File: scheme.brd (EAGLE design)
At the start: 100 x 80 mm, 49 parts, among them J1 22-05-7048-04, J2 22-05-7028-02

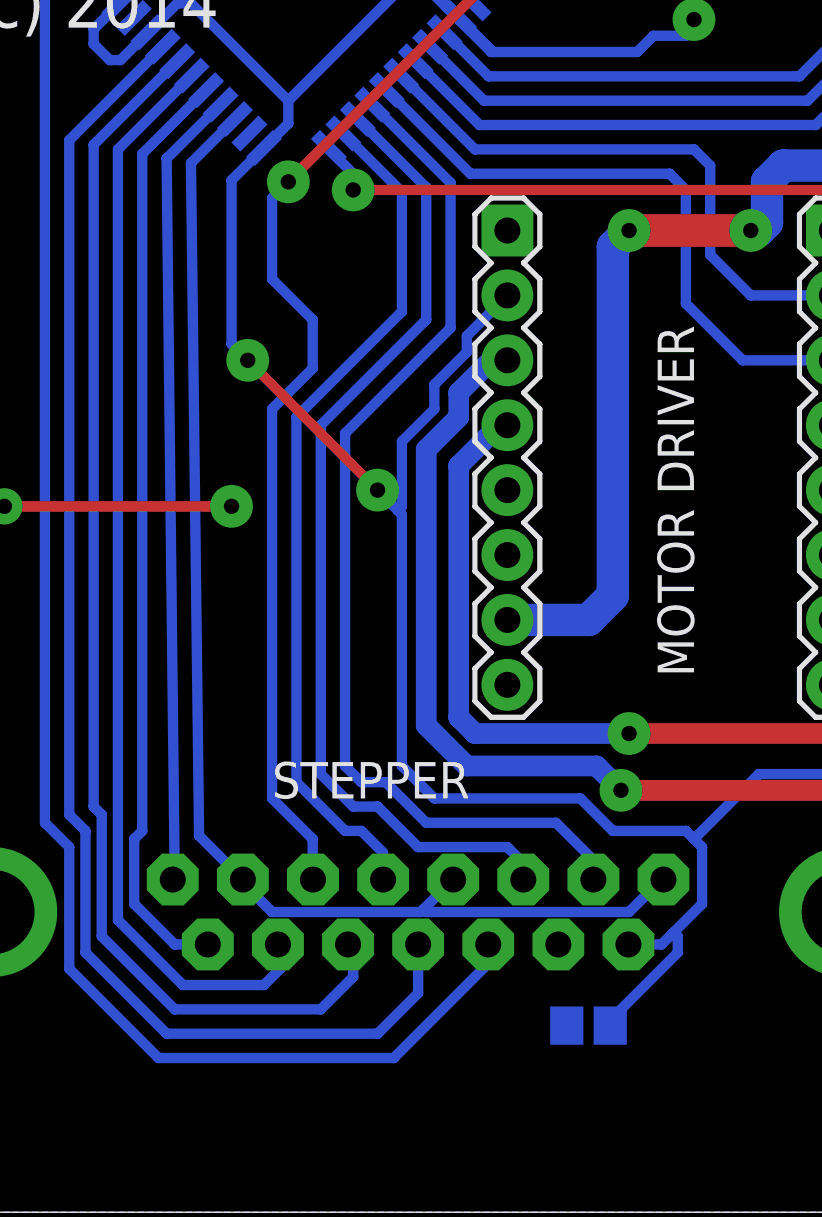
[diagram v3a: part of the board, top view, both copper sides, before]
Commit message: Fix DB-15 connector pinout for driver
Signed-off-by: Nikita 'webconn' Maslov <wkernelteam@gmail.com>
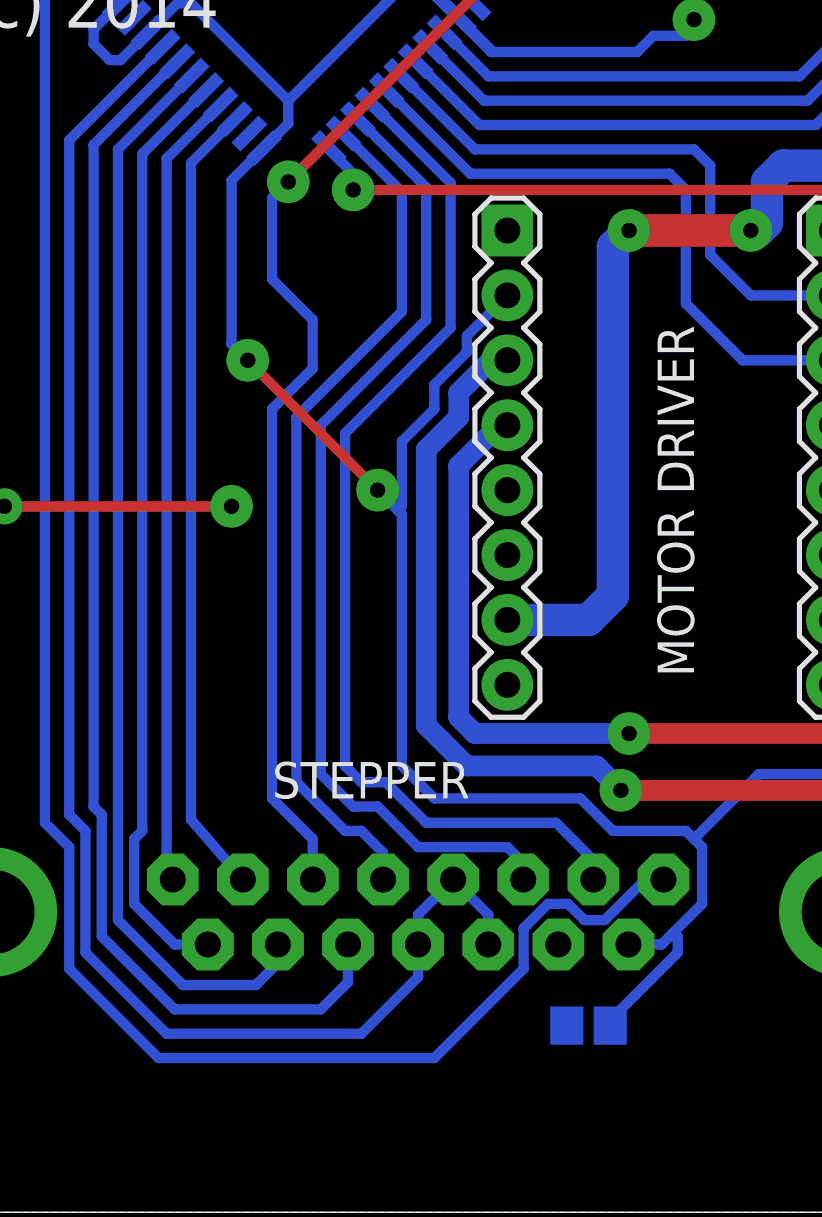
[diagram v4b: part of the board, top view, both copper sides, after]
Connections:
- net RELAY renamed SY_STEP
- net X_DIR renamed SX_STEP
- net X_STEP renamed S_ENABLE
- net Y_DIR renamed SZ_DIR
- net Y_LIM renamed SX_DIR
- net Z_DIR renamed SZ_LIM
- net Z_LIM renamed SY_DIR
- net Z_STEP renamed SY_LIM
- removed net ENABLE: U$1.36, X2.2, X2.5, X2.8
- removed net STOP: U$1.1, X2.13
- removed net Y_STEP: U$1.41, X2.12
- new net SX_LIM: U$1.1, X2.8
- new net SZ_STEP: U$1.36, X2.2
- new net S_RELAY: U$1.41, X2.12, X2.13, X2.5
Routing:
- net SX_LIM: track 0.00 -> 73.3 mm
- net STOP: track 64.4 -> 0.00 mm
- net S_RELAY: track 0.00 -> 60.0 mm
- net Y_STEP: track 54.1 -> 0.00 mm
- net ENABLE: track 50.5 -> 0.00 mm
- net SZ_STEP: track 0.00 -> 31.2 mm

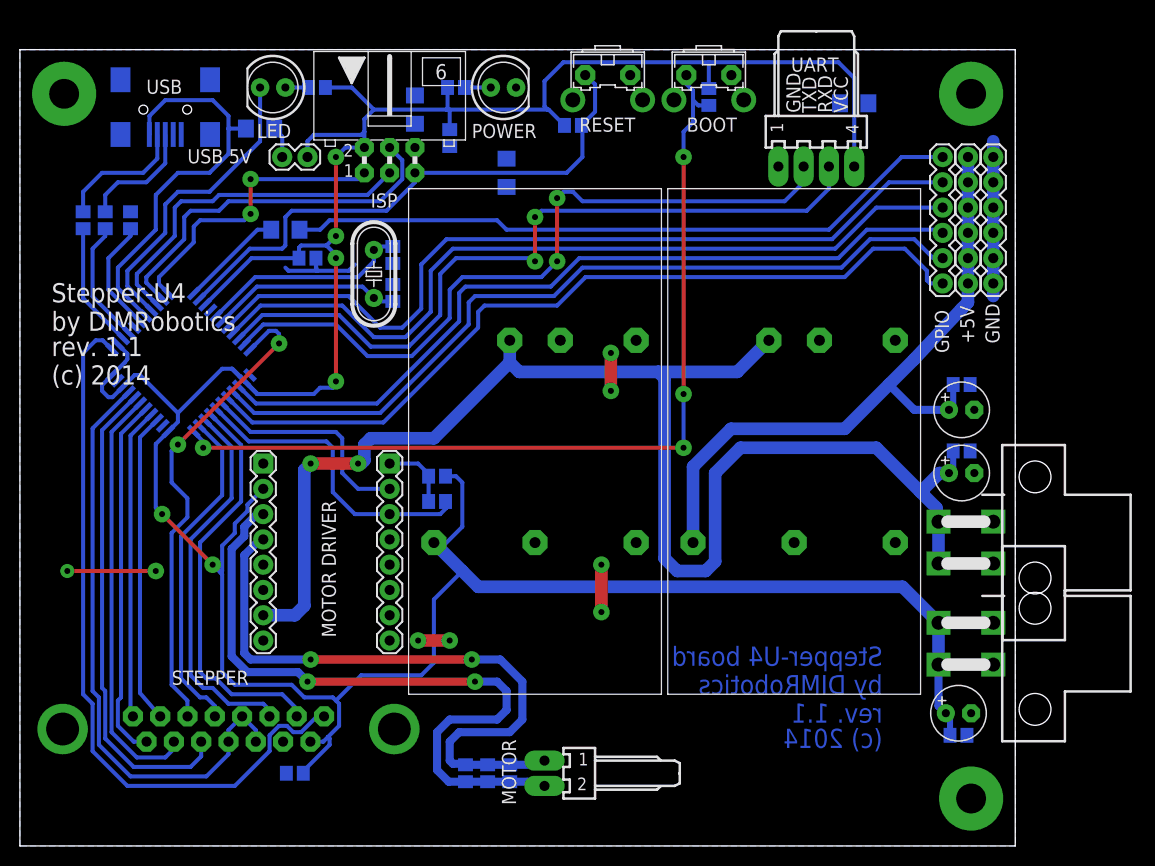
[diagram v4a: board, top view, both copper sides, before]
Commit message: Add D-SUB power jumper
Signed-off-by: Nikita 'webconn' Maslov <wkernelteam@gmail.com>
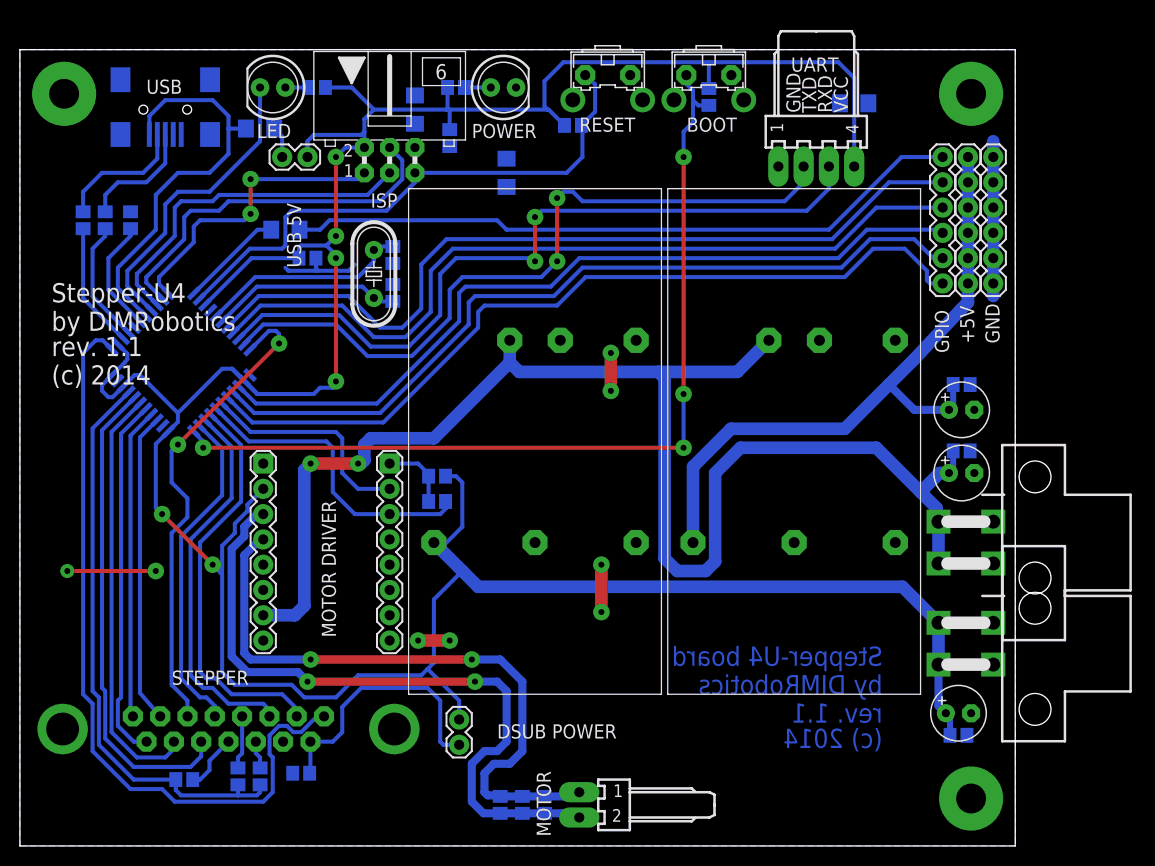
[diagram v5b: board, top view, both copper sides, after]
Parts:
- added JP7: M02PTH, SparkFun-Connectors:1X02
- added R14, R15, R16: 0, resistor:R0805
- moved C13 4.72 mm to (52.7, 4.13)
- moved C14 4.72 mm to (50.5, 4.13)
- moved C15 4.72 mm to (48.3, 4.13)
- moved J2 4.72 mm to (56.2, 4.13)
- moved C5 0.64 mm to (28.3, 7.30)
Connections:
- new net N$16: C5.2, JP7.2, X2.15
- new net S_RELAY1: R14.1, X2.5
- new net S_RELAY2: R15.1, X2.13
- new net S_RELAY3: R16.1, X2.12
- net S_RELAY: now also R14.2, R15.2, R16.2; no longer X2.12, X2.13, X2.5
- net VCC: now also JP7.1; no longer C5.2, X2.15
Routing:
- net N$16: track 0.00 -> 26.7 mm
- net S_RELAY3: track 0.00 -> 5.73 mm
- net S_RELAY1: track 0.00 -> 5.36 mm
- net VCC: track 331.1 -> 326.2 mm
- net SX_LIM: track 73.3 -> 77.5 mm
- net S_RELAY2: track 0.00 -> 2.82 mm
- net S_RELAY: track 60.0 -> 58.1 mm
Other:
- board text added: "DSUB POWER"
